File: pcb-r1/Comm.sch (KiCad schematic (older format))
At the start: 12 parts, among them P201 CONN_01X06, P202 CONN_01X04, P203 CONN_01X04, P204 CONN_01X03, P205 CONN_01X02, SW201 SW_PUSH

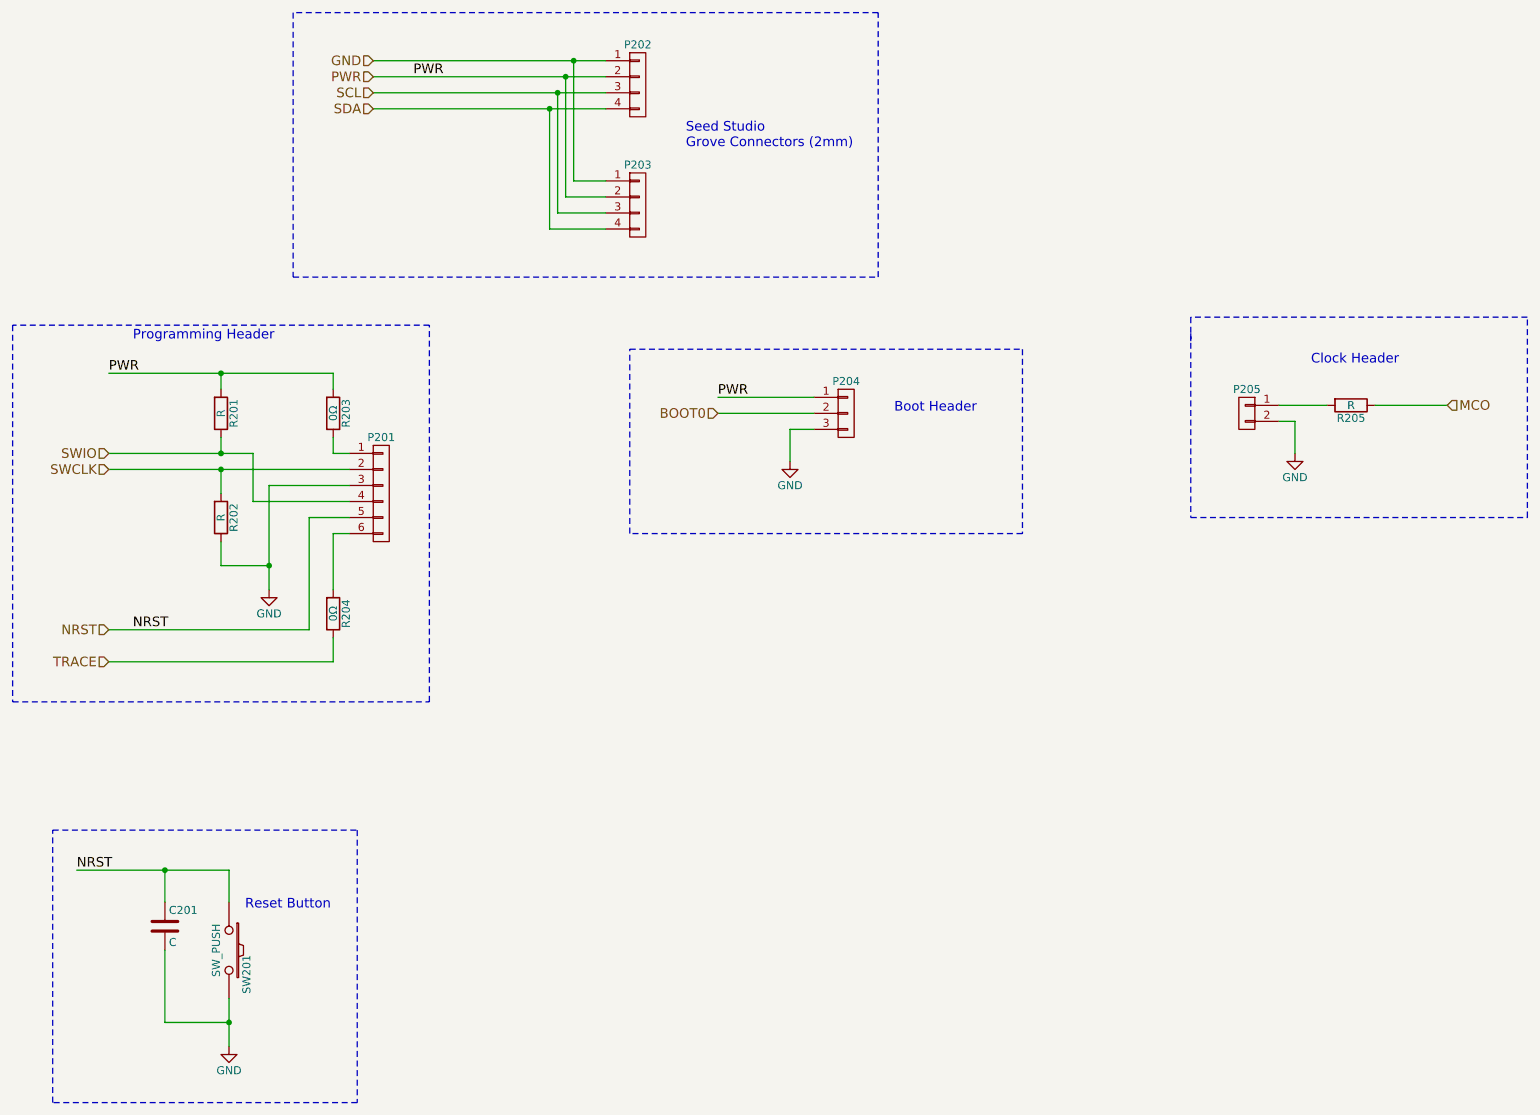
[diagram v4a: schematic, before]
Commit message: Corrected the symbol and footprint for the reset switch
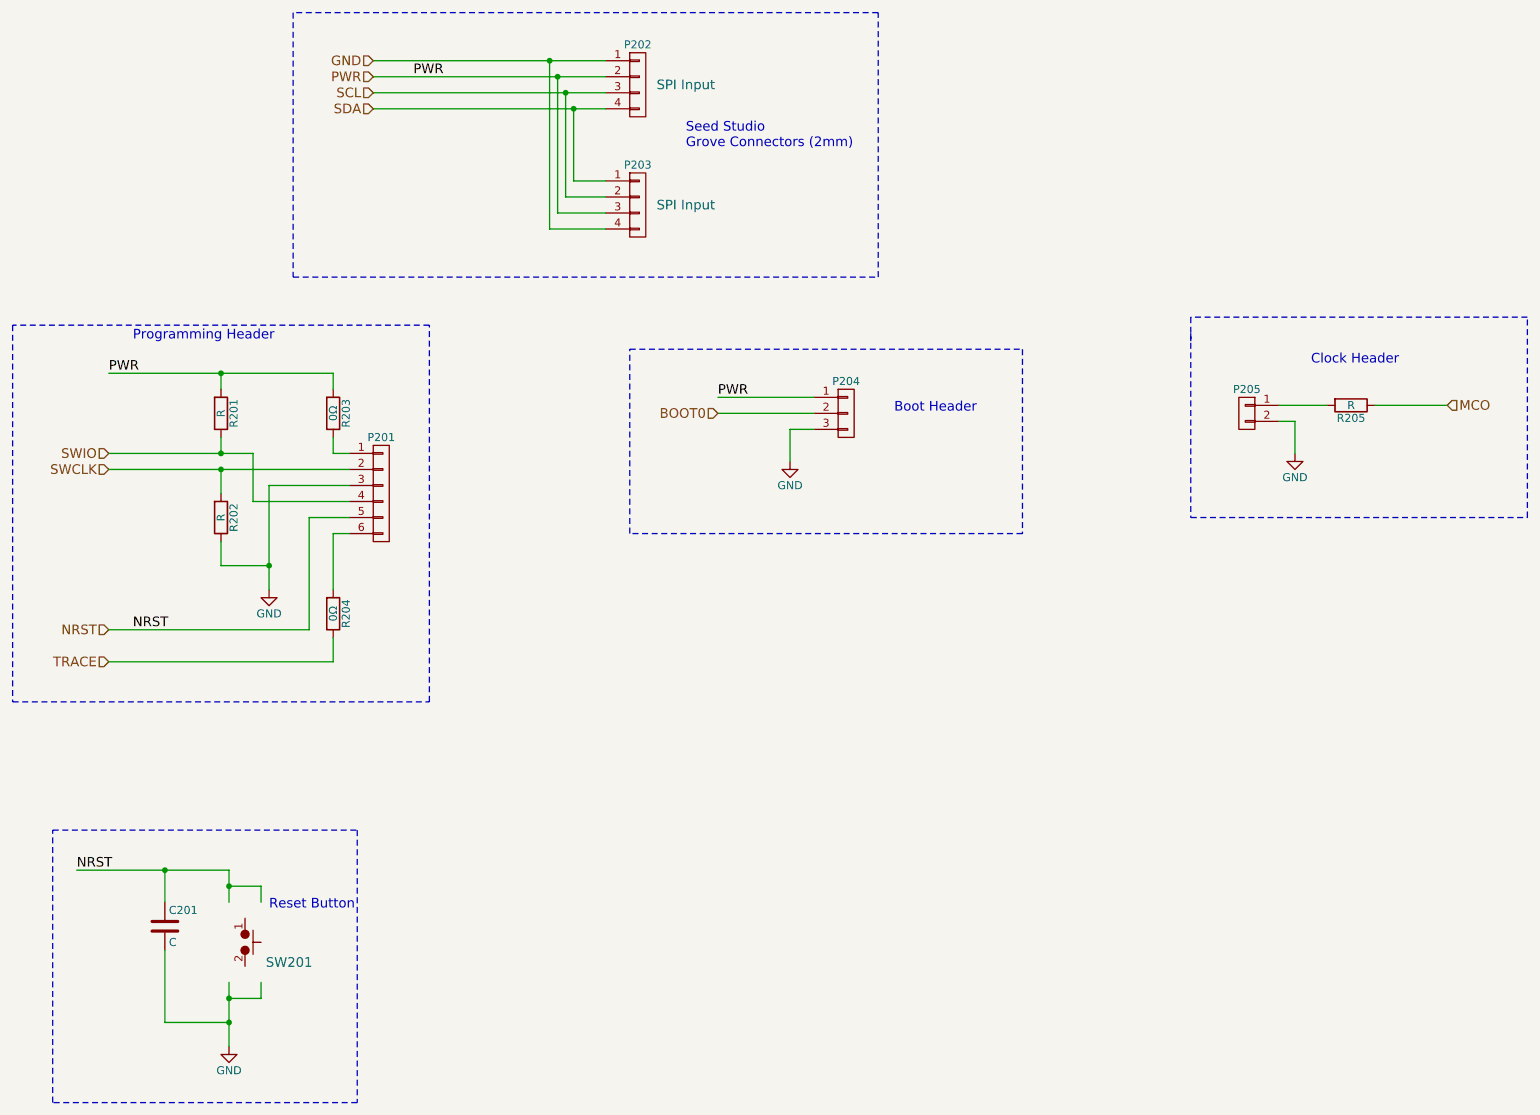
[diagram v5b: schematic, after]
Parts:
- removed SW201: SW_PUSH, CentralCommand:PTS525SM15SMTR2LFS, symbol SW_PUSH
- added SW201: TL3315NF160Q, CentralCommand:PTS525SM15SMTR2LFS, symbol TL3315NF160Q
- P202, P203: ConradPN (none) -> Value; Label (none) -> SPI Input; MPN (none) -> Value
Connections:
- wire segments 48 -> 52
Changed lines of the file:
@@
-$EndComp
-$Comp
-L SW_PUSH SW201
-U 1 1 56673C7E
-P 2350 6600
-F 0 "SW201" H 2500 6710 50  0000 C CNN
-F 1 "SW_PUSH" H 2350 6520 50  0000 C CNN
-F 2 "CentralCommand:PTS525SM15SMTR2LFS" H 2350 6600 60  0001 C CNN
-F 3 "" H 2350 6600 60  0000 C CNN
-	1    2350 6600
-	0    1    1    0
 $EndComp
 $Comp
@@
 	1    0    0    -1
 $EndComp
-Text Notes 2450 6350 0    60   ~ 0
+Text Notes 2600 6350 0    60   ~ 0
 Reset Button
 Text Label 1400 6100 0    60   ~ 0
@@
 F 2 "CentralCommand:Grove-2mm" H 4900 1200 60  0001 C CNN
 F 3 "" H 4900 1200 60  0000 C CNN
+F 4 "Value" H 4900 1200 60  0001 C CNN "MPN"
+F 5 "Value" H 4900 1200 60  0001 C CNN "ConradPN"
+F 6 "SPI Input" H 5200 1200 60  0000 C CNN "Label"
 	1    4900 1200
 	1    0    0    -1
@@
 Connection ~ 1950 6100
 Wire Wire Line
-	2350 6900 2350 7200
+	2350 6800 2350 7200
 Wire Wire Line
 	1950 6600 1950 7050
@@
 F 2 "CentralCommand:Grove-2mm" H 4900 1950 60  0001 C CNN
 F 3 "" H 4900 1950 60  0000 C CNN
+F 4 "Value" H 4900 1950 60  0001 C CNN "MPN"
+F 5 "Value" H 4900 1950 60  0001 C CNN "ConradPN"
+F 6 "SPI Input" H 5200 1950 60  0000 C CNN "Label"
 	1    4900 1950
 	1    0    0    -1
 $EndComp
 Wire Wire Line
-	4500 1050 4500 1800
-Wire Wire Line
 	4500 1800 4700 1800
-Connection ~ 4500 1050
-Wire Wire Line
-	4450 1150 4450 1900
 Wire Wire Line
 	4450 1900 4700 1900
-Connection ~ 4450 1150
-Wire Wire Line
-	4400 1250 4400 2000
 Wire Wire Line
 	4400 2000 4700 2000
-Connection ~ 4400 1250
-Wire Wire Line
-	4350 1350 4350 2100
 Wire Wire Line
 	4350 2100 4700 2100
-Connection ~ 4350 1350
 Text Notes 5200 1600 0    60   ~ 0
 Seed Studio \nGrove Connectors (2mm)
@@
 Text Label 3500 1150 0    60   ~ 0
 PWR
+$Comp
+L TL3315NF160Q SW201
+U 1 1 566C72BD
+P 2450 6550
+F 0 "SW201" H 2725 6425 60  0000 C CNN
+F 1 "TL3315NF160Q" H 2950 6550 60  0001 C CNN
+F 2 "CentralCommand:PTS525SM15SMTR2LFS" H 2450 6500 60  0001 C CNN
+F 3 "" H 2450 6500 60  0000 C CNN
+	1    2450 6550
+	1    0    0    -1
+$EndComp
+Wire Wire Line
+	2350 6900 2550 6900
+Wire Wire Line
+	2550 6900 2550 6800
+Connection ~ 2350 6900
+Wire Wire Line
+	2350 6200 2550 6200
+Wire Wire Line
+	2550 6200 2550 6300
+Connection ~ 2350 6200
+Wire Wire Line
+	4500 1800 4500 1350
+Connection ~ 4500 1350
+Wire Wire Line
+	4450 1900 4450 1250
+Connection ~ 4450 1250
+Wire Wire Line
+	4400 2000 4400 1150
+Connection ~ 4400 1150
+Wire Wire Line
+	4350 2100 4350 1050
+Connection ~ 4350 1050
 $EndSCHEMATC

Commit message: Intermediate save of the layout
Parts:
- added R206, R207, R208, R209: 0Ω, Resistors_SMD:R_0805, symbol R
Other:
- moved on the sheet: SW201
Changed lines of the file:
@@
 $EndComp
 $Comp
-L GND #PWR06
+L GND #PWR07
 U 1 1 56673C8A
 P 2350 7200
-F 0 "#PWR06" H 2350 6950 50  0001 C CNN
+F 0 "#PWR07" H 2350 6950 50  0001 C CNN
 F 1 "GND" H 2350 7050 50  0000 C CNN
 F 2 "" H 2350 7200 60  0000 C CNN
@@
 	1    0    0    -1
 $EndComp
-Text Notes 2600 6350 0    60   ~ 0
+Text Notes 2450 6300 0    60   ~ 0
 Reset Button
 Text Label 1400 6100 0    60   ~ 0
@@
 $EndComp
 $Comp
-L GND #PWR07
+L GND #PWR08
 U 1 1 56674184
 P 2600 4350
-F 0 "#PWR07" H 2600 4100 50  0001 C CNN
+F 0 "#PWR08" H 2600 4100 50  0001 C CNN
 F 1 "GND" H 2600 4200 50  0000 C CNN
 F 2 "" H 2600 4350 60  0000 C CNN
@@
 Connection ~ 1950 6100
 Wire Wire Line
-	2350 6800 2350 7200
-Wire Wire Line
 	1950 6600 1950 7050
 Wire Wire Line
@@
 	4500 1800 4700 1800
 Wire Wire Line
-	4450 1900 4700 1900
-Wire Wire Line
-	4400 2000 4700 2000
-Wire Wire Line
-	4350 2100 4700 2100
+	4350 1900 4700 1900
+Wire Wire Line
+	4200 2000 4700 2000
+Wire Wire Line
+	4050 2100 4700 2100
 Text Notes 5200 1600 0    60   ~ 0
 Seed Studio \nGrove Connectors (2mm)
@@
 PWR
 $Comp
-L GND #PWR08
+L GND #PWR09
 U 1 1 56674C0D
 P 5850 3550
-F 0 "#PWR08" H 5850 3300 50  0001 C CNN
+F 0 "#PWR09" H 5850 3300 50  0001 C CNN
 F 1 "GND" H 5850 3400 50  0000 C CNN
 F 2 "" H 5850 3550 60  0000 C CNN
@@
 	8900 3200 9200 3200
 $Comp
-L GND #PWR09
+L GND #PWR010
 U 1 1 56674E8A
 P 9000 3500
-F 0 "#PWR09" H 9000 3250 50  0001 C CNN
+F 0 "#PWR010" H 9000 3250 50  0001 C CNN
 F 1 "GND" H 9000 3350 50  0000 C CNN
 F 2 "" H 9000 3500 60  0000 C CNN
@@
 L TL3315NF160Q SW201
 U 1 1 566C72BD
-P 2450 6550
-F 0 "SW201" H 2725 6425 60  0000 C CNN
-F 1 "TL3315NF160Q" H 2950 6550 60  0001 C CNN
-F 2 "CentralCommand:PTS525SM15SMTR2LFS" H 2450 6500 60  0001 C CNN
-F 3 "" H 2450 6500 60  0000 C CNN
-	1    2450 6550
-	1    0    0    -1
-$EndComp
-Wire Wire Line
-	2350 6900 2550 6900
-Wire Wire Line
-	2550 6900 2550 6800
-Connection ~ 2350 6900
-Wire Wire Line
-	2350 6200 2550 6200
-Wire Wire Line
-	2550 6200 2550 6300
-Connection ~ 2350 6200
-Wire Wire Line
-	4500 1800 4500 1350
+P 2350 6450
+F 0 "SW201" H 2625 6325 60  0000 C CNN
+F 1 "TL3315NF160Q" H 2850 6450 60  0001 C CNN
+F 2 "CentralCommand:PTS525SM15SMTR2LFS" H 2350 6400 60  0001 C CNN
+F 3 "" H 2350 6400 60  0000 C CNN
+	1    2350 6450
+	1    0    0    -1
+$EndComp
+Wire Wire Line
+	2350 6600 2350 7200
+$Comp
+L R R209
+U 1 1 567ECC7A
+P 4500 1550
+F 0 "R209" V 4580 1550 50  0000 C CNN
+F 1 "0Ω" V 4500 1550 50  0000 C CNN
+F 2 "Resistors_SMD:R_0805" V 4430 1550 30  0001 C CNN
+F 3 "" H 4500 1550 30  0000 C CNN
+	1    4500 1550
+	1    0    0    1
+$EndComp
+$Comp
+L R R208
+U 1 1 567ECDA6
+P 4350 1550
+F 0 "R208" V 4430 1550 50  0000 C CNN
+F 1 "0Ω" V 4350 1550 50  0000 C CNN
+F 2 "Resistors_SMD:R_0805" V 4280 1550 30  0001 C CNN
+F 3 "" H 4350 1550 30  0000 C CNN
+	1    4350 1550
+	1    0    0    1
+$EndComp
+$Comp
+L R R207
+U 1 1 567ECDE6
+P 4200 1550
+F 0 "R207" V 4280 1550 50  0000 C CNN
+F 1 "0Ω" V 4200 1550 50  0000 C CNN
+F 2 "Resistors_SMD:R_0805" V 4130 1550 30  0001 C CNN
+F 3 "" H 4200 1550 30  0000 C CNN
+	1    4200 1550
+	1    0    0    1
+$EndComp
+$Comp
+L R R206
+U 1 1 567ECE34
+P 4050 1550
+F 0 "R206" V 4130 1550 50  0000 C CNN
+F 1 "0Ω" V 4050 1550 50  0000 C CNN
+F 2 "Resistors_SMD:R_0805" V 3980 1550 30  0001 C CNN
+F 3 "" H 4050 1550 30  0000 C CNN
+	1    4050 1550
+	1    0    0    1
+$EndComp
+Wire Wire Line
+	4500 1800 4500 1700
+Wire Wire Line
+	4350 1700 4350 1900
+Wire Wire Line
+	4200 1700 4200 2000
+Wire Wire Line
+	4050 1700 4050 2100
+Wire Wire Line
+	4500 1400 4500 1350
 Connection ~ 4500 1350
 Wire Wire Line
-	4450 1900 4450 1250
-Connection ~ 4450 1250
-Wire Wire Line
-	4400 2000 4400 1150
-Connection ~ 4400 1150
-Wire Wire Line
-	4350 2100 4350 1050
-Connection ~ 4350 1050
+	4350 1400 4350 1250
+Connection ~ 4350 1250
+Wire Wire Line
+	4200 1400 4200 1150
+Connection ~ 4200 1150
+Wire Wire Line
+	4050 1400 4050 1050
+Connection ~ 4050 1050
 $EndSCHEMATC

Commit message: Final draft layout. Published to build log as V01
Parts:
- P202: Label SPI Input -> SPI Output
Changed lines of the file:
@@
 F 4 "Value" H 4900 1200 60  0001 C CNN "MPN"
 F 5 "Value" H 4900 1200 60  0001 C CNN "ConradPN"
-F 6 "SPI Input" H 5200 1200 60  0000 C CNN "Label"
+F 6 "SPI Output" H 5200 1200 60  0000 C CNN "Label"
 	1    4900 1200
 	1    0    0    -1

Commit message: Completed the layout. Saving before sending off to Fab.
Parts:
- removed P205: CONN_01X02, Pin_Headers:Pin_Header_Straight_1x02, symbol CONN_01X02
- removed R205: R, Resistors_SMD:R_0805, symbol R
- P202: Label SPI Output -> SPI Input
- P203: Label SPI Input -> SPI Output
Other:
- note removed: "Clock Header"
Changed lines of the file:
@@
 F 4 "Value" H 4900 1200 60  0001 C CNN "MPN"
 F 5 "Value" H 4900 1200 60  0001 C CNN "ConradPN"
-F 6 "SPI Output" H 5200 1200 60  0000 C CNN "Label"
+F 6 "SPI Input" H 5200 1200 60  0000 C CNN "Label"
 	1    4900 1200
 	1    0    0    -1
@@
 F 4 "Value" H 4900 1950 60  0001 C CNN "MPN"
 F 5 "Value" H 4900 1950 60  0001 C CNN "ConradPN"
-F 6 "SPI Input" H 5200 1950 60  0000 C CNN "Label"
+F 6 "SPI Output" H 5200 1950 60  0000 C CNN "Label"
 	1    4900 1950
 	1    0    0    -1
@@
 Text HLabel 5400 3250 0    60   Input ~ 0
 BOOT0
-$Comp
-L CONN_01X02 P205
-U 1 1 56674C8F
-P 8700 3250
-F 0 "P205" H 8700 3400 50  0000 C CNN
-F 1 "CONN_01X02" V 8800 3250 50  0001 C CNN
-F 2 "Pin_Headers:Pin_Header_Straight_1x02" H 8700 3250 60  0001 C CNN
-F 3 "" H 8700 3250 60  0000 C CNN
-	1    8700 3250
-	-1   0    0    -1
-$EndComp
-$Comp
-L R R205
-U 1 1 56674D50
-P 9350 3200
-F 0 "R205" V 9430 3200 50  0000 C CNN
-F 1 "R" V 9350 3200 50  0000 C CNN
-F 2 "Resistors_SMD:R_0805" V 9280 3200 30  0001 C CNN
-F 3 "" H 9350 3200 30  0000 C CNN
-	1    9350 3200
-	0    1    1    0
-$EndComp
-Wire Wire Line
-	9500 3200 9950 3200
-Text HLabel 9950 3200 2    60   Input ~ 0
-MCO
-Wire Wire Line
-	8900 3200 9200 3200
-$Comp
-L GND #PWR010
-U 1 1 56674E8A
-P 9000 3500
-F 0 "#PWR010" H 9000 3250 50  0001 C CNN
-F 1 "GND" H 9000 3350 50  0000 C CNN
-F 2 "" H 9000 3500 60  0000 C CNN
-F 3 "" H 9000 3500 60  0000 C CNN
-	1    9000 3500
-	1    0    0    -1
-$EndComp
-Wire Wire Line
-	8900 3300 9000 3300
-Wire Wire Line
-	9000 3300 9000 3500
-Text Notes 9100 2950 0    60   ~ 0
-Clock Header
 Text Notes 6500 3250 0    60   ~ 0
 Boot Header
@@
 	4850 4000 4850 2850
 Wire Notes Line
-	8350 2750 8350 3900
-Wire Notes Line
-	8350 3900 10450 3900
-Wire Notes Line
-	10450 3900 10450 2650
-Wire Notes Line
-	10450 2650 8350 2650
-Wire Notes Line
-	8350 2650 8350 2800
-Wire Notes Line
 	1250 5850 3150 5850
